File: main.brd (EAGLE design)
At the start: 53.3 x 68.6 mm, 36 parts, among them IC1 4050D, U1 MCP2551, U2 STN1100

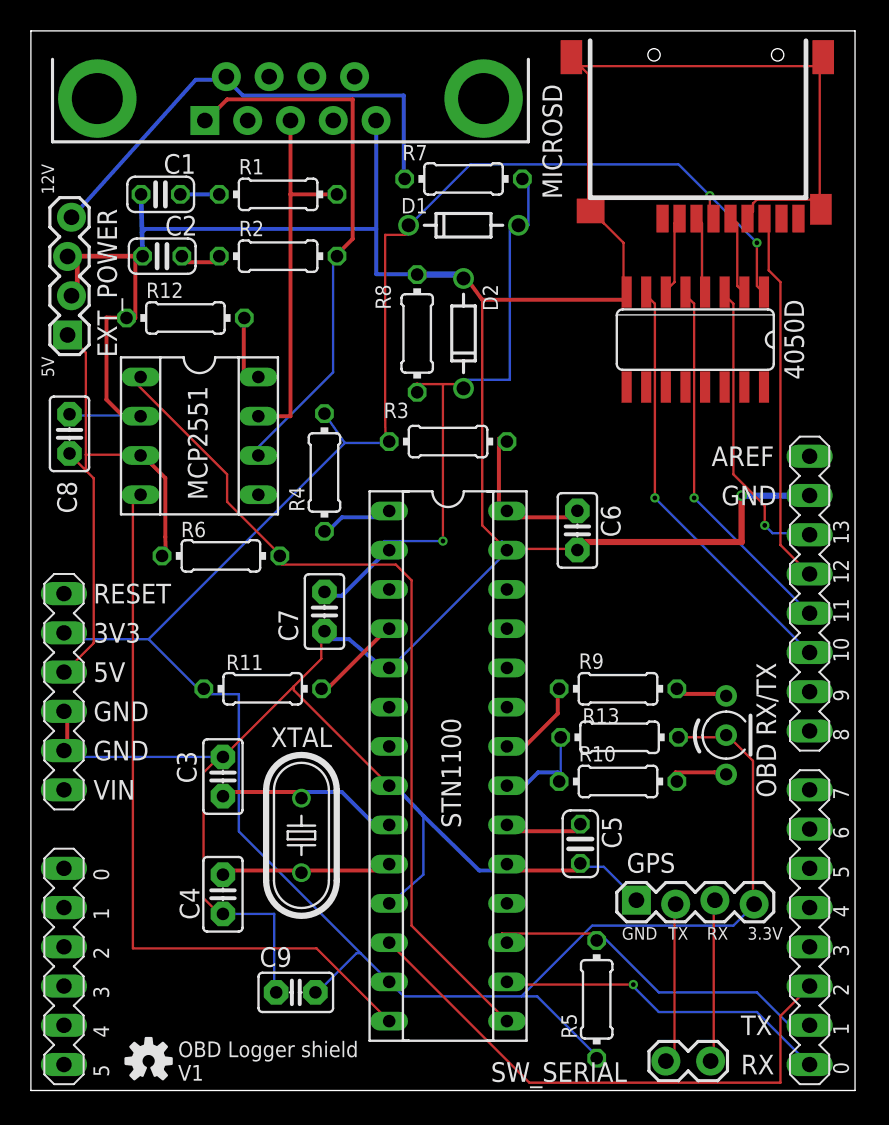
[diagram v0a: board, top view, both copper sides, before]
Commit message: Fixed errors on UART tx/rx
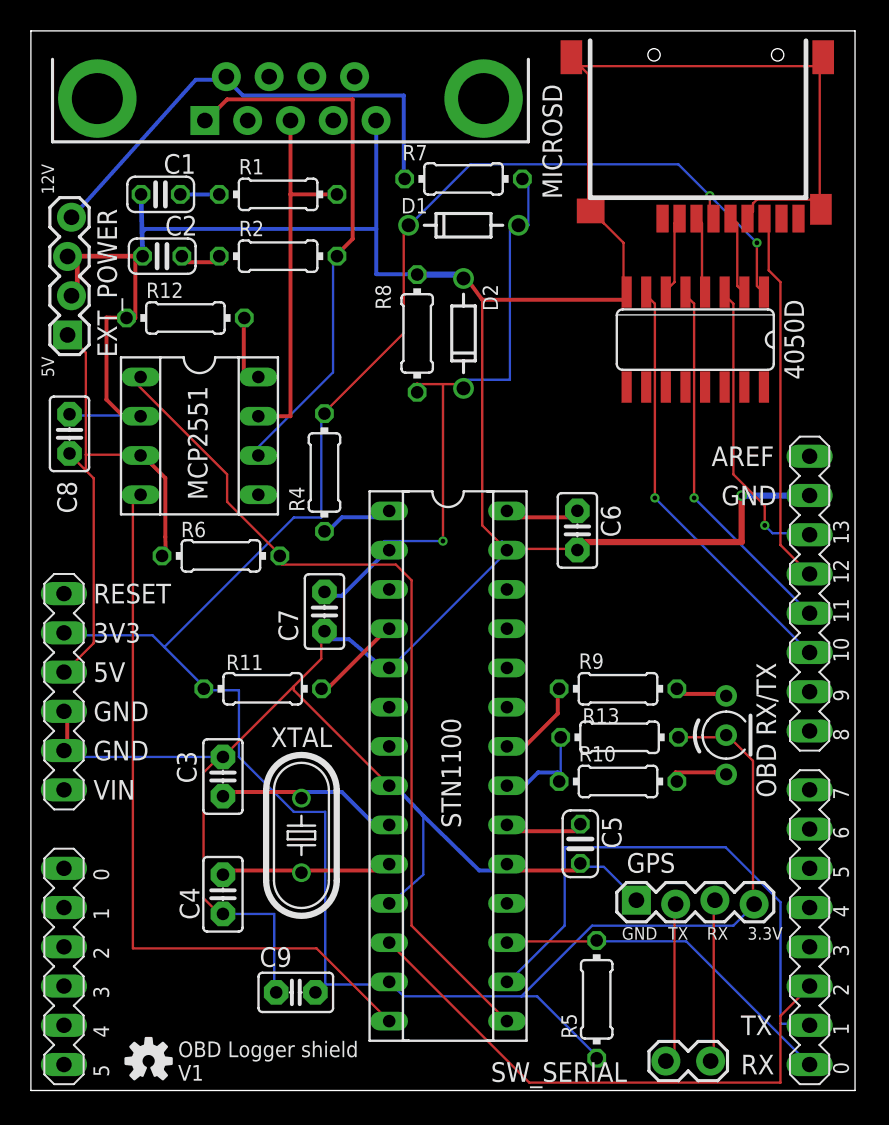
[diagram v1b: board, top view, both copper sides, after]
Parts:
- removed R3: 10, resistor:0204/7
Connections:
- net 3.3V: no longer R3.2
- net N$9: no longer R3.1
- net UART_RX: now also ARDUINO1.01; no longer ARDUINO1.00
- net UART_TX: now also ARDUINO1.00; no longer ARDUINO1.01
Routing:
- net UART_RX: track 21.9 -> 35.5 mm, vias 1 -> 0
- net N$9: track 11.4 -> 5.08 mm
- net 3.3V: track 158.6 -> 154.7 mm
- net UART_TX: track 24.3 -> 22.9 mm
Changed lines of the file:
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@@
 <element name="C5" library="rcl" package="C025-024X044" value="10uF" x="35.56" y="15.97" rot="R270"/>
 <element name="C6" library="capacitor-wima" package="C2.5-2" value="1uF" x="35.37" y="36.25" rot="R270"/>
-<element name="R3" library="resistor" package="0204/7" value="10" x="27" y="42" smashed="yes" rot="R180">
-<attribute name="NAME" x="24.46" y="44.5146" size="0.9906" layer="25" ratio="10" rot="R180"/>
-<attribute name="VALUE" x="28.6256" y="42.4826" size="0.9906" layer="27" ratio="10" rot="R180"/>
-</element>
 <element name="R4" library="resistor" package="0204/7" value="10k" x="19" y="40" rot="R90"/>
 <element name="R5" library="resistor" package="0204/7" value="1k" x="36.62" y="5.9" rot="R90"/>
@@
 <contactref element="ARDUINO1" pad="3V3"/>
 <contactref element="U2" pad="13"/>
-<contactref element="R3" pad="2"/>
 <contactref element="R4" pad="2"/>
 <contactref element="R5" pad="1"/>
@@
 <contactref element="IC1" pad="1"/>
 <contactref element="U$1" pad="4"/>
-<wire x1="7.62" y1="29.21" x2="11.176" y2="25.654" width="0.1524" layer="16"/>
-<wire x1="11.176" y1="25.654" x2="11.23" y2="25.6" width="0.1524" layer="16"/>
-<wire x1="2.54" y1="29.21" x2="7.62" y2="29.21" width="0.1524" layer="16"/>
-<wire x1="11.23" y1="25.6" x2="11.19" y2="26" width="0.1524" layer="16"/>
-<wire x1="2.54" y1="29.21" x2="2.14" y2="29.62" width="0.1524" layer="16"/>
-<wire x1="22.93" y1="43.48" x2="22.96" y2="41.91" width="0.1524" layer="1"/>
-<wire x1="22.93" y1="55.38" x2="22.93" y2="43.48" width="0.1524" layer="1"/>
-<wire x1="22.96" y1="41.91" x2="23.19" y2="42" width="0.1524" layer="1"/>
-<wire x1="22.93" y1="55.38" x2="24.4" y2="55.38" width="0.1524" layer="1"/>
-<wire x1="24.4" y1="55.38" x2="24.4" y2="55.8" width="0.1524" layer="1"/>
-<wire x1="24.4" y1="55.8" x2="24.444" y2="56" width="0.1524" layer="1"/>
-<wire x1="20.32" y1="41.91" x2="7.62" y2="29.21" width="0.1524" layer="16"/>
-<wire x1="22.86" y1="41.91" x2="20.32" y2="41.91" width="0.1524" layer="16"/>
-<wire x1="22.86" y1="41.91" x2="23.19" y2="42" width="0.1524" layer="16"/>
-<wire x1="20.32" y1="41.91" x2="19" y2="43.81" width="0.1524" layer="16"/>
-<wire x1="13.462" y1="16.764" x2="21.336" y2="8.89" width="0.1524" layer="16"/>
-<wire x1="21.336" y1="8.89" x2="23.114" y2="7.112" width="0.1524" layer="16"/>
-<wire x1="13.462" y1="25.654" x2="13.462" y2="16.764" width="0.1524" layer="16"/>
-<wire x1="11.176" y1="25.654" x2="13.462" y2="25.654" width="0.1524" layer="16"/>
-<wire x1="23.114" y1="7.112" x2="23.19" y2="7.03" width="0.1524" layer="16"/>
-<wire x1="11.176" y1="25.654" x2="11.19" y2="26" width="0.1524" layer="16"/>
 <wire x1="43.942" y1="57.912" x2="43.942" y2="56.642" width="0.1524" layer="1"/>
 <wire x1="41.91" y1="59.944" x2="43.942" y2="57.912" width="0.1524" layer="16"/>
@@
 <wire x1="46.736" y1="11.938" x2="46.81" y2="12.063" width="0.1524" layer="16"/>
 <contactref element="C9" pad="1"/>
-<wire x1="21.082" y1="8.89" x2="18.542" y2="6.35" width="0.1524" layer="16"/>
-<wire x1="21.336" y1="8.89" x2="21.082" y2="8.89" width="0.1524" layer="16"/>
+<wire x1="24.13" y1="49.022" x2="19.05" y2="43.942" width="0.1524" layer="1"/>
+<wire x1="24.13" y1="55.626" x2="24.13" y2="49.022" width="0.1524" layer="1"/>
+<wire x1="24.384" y1="55.88" x2="24.13" y2="55.626" width="0.1524" layer="1"/>
+<wire x1="19.05" y1="43.942" x2="19" y2="43.81" width="0.1524" layer="1"/>
+<wire x1="24.384" y1="55.88" x2="24.444" y2="56" width="0.1524" layer="1"/>
+<wire x1="19.05" y1="6.858" x2="18.542" y2="6.35" width="0.1524" layer="16"/>
+<wire x1="23.114" y1="6.858" x2="19.05" y2="6.858" width="0.1524" layer="16"/>
 <wire x1="18.542" y1="6.35" x2="18.415" y2="6.35" width="0.1524" layer="16"/>
+<wire x1="23.114" y1="6.858" x2="23.19" y2="7.03" width="0.1524" layer="16"/>
+<wire x1="7.874" y1="29.464" x2="8.636" y2="28.702" width="0.1524" layer="16"/>
+<wire x1="8.636" y1="28.702" x2="11.176" y2="26.162" width="0.1524" layer="16"/>
+<wire x1="2.286" y1="29.464" x2="7.874" y2="29.464" width="0.1524" layer="16"/>
+<wire x1="11.176" y1="26.162" x2="11.19" y2="26" width="0.1524" layer="16"/>
+<wire x1="2.286" y1="29.464" x2="2.14" y2="29.62" width="0.1524" layer="16"/>
+<wire x1="19.05" y1="18.034" x2="19.05" y2="6.858" width="0.1524" layer="16"/>
+<wire x1="17.018" y1="18.034" x2="19.05" y2="18.034" width="0.1524" layer="16"/>
+<wire x1="13.462" y1="21.59" x2="17.018" y2="18.034" width="0.1524" layer="16"/>
+<wire x1="13.462" y1="25.908" x2="13.462" y2="21.59" width="0.1524" layer="16"/>
+<wire x1="11.43" y1="25.908" x2="13.462" y2="25.908" width="0.1524" layer="16"/>
+<wire x1="11.43" y1="25.908" x2="11.19" y2="26" width="0.1524" layer="16"/>
+<wire x1="18.796" y1="37.084" x2="18.796" y2="43.688" width="0.1524" layer="16"/>
+<wire x1="17.018" y1="37.084" x2="18.796" y2="37.084" width="0.1524" layer="16"/>
+<wire x1="8.636" y1="28.702" x2="17.018" y2="37.084" width="0.1524" layer="16"/>
+<wire x1="18.796" y1="43.688" x2="19" y2="43.81" width="0.1524" layer="16"/>
 </signal>
 <signal name="CAN_TX">
@@
 <contactref element="C6" pad="1"/>
 <contactref element="U2" pad="28"/>
-<contactref element="R3" pad="1"/>
 <wire x1="35.37" y1="37.1" x2="31.56" y2="37.1" width="0.254" layer="1"/>
 <wire x1="31.56" y1="37.1" x2="30.81" y2="37.51" width="0.254" layer="1"/>
 <wire x1="35.37" y1="37.1" x2="35.37" y2="37.52" width="0.254" layer="1"/>
-<wire x1="30.29" y1="37.1" x2="30.29" y2="42.18" width="0.254" layer="1"/>
-<wire x1="30.29" y1="42.18" x2="30.81" y2="42" width="0.254" layer="1"/>
-<wire x1="30.29" y1="37.1" x2="30.81" y2="37.51" width="0.254" layer="1"/>
 </signal>
 <signal name="N$8">
@@
 <contactref element="U2" pad="17"/>
 <contactref element="R5" pad="2"/>
-<contactref element="ARDUINO1" pad="01"/>
-<wire x1="36.83" y1="10.16" x2="30.48" y2="10.16" width="0.1524" layer="1"/>
-<wire x1="30.48" y1="10.16" x2="30.81" y2="9.57" width="0.1524" layer="1"/>
-<wire x1="36.83" y1="10.16" x2="36.62" y2="9.71" width="0.1524" layer="1"/>
-<wire x1="46.99" y1="6.35" x2="49.53" y2="3.81" width="0.1524" layer="16"/>
-<wire x1="40.64" y1="6.35" x2="46.99" y2="6.35" width="0.1524" layer="16"/>
-<wire x1="36.83" y1="10.16" x2="40.64" y2="6.35" width="0.1524" layer="16"/>
-<wire x1="49.53" y1="3.81" x2="50.4" y2="4.22" width="0.1524" layer="16"/>
-<wire x1="36.83" y1="10.16" x2="36.62" y2="9.71" width="0.1524" layer="16"/>
+<contactref element="ARDUINO1" pad="00"/>
+<wire x1="36.576" y1="9.652" x2="30.988" y2="9.652" width="0.1524" layer="1"/>
+<wire x1="30.988" y1="9.652" x2="30.81" y2="9.57" width="0.1524" layer="1"/>
+<wire x1="36.576" y1="9.652" x2="36.62" y2="9.71" width="0.1524" layer="1"/>
+<wire x1="42.418" y1="9.652" x2="50.292" y2="1.778" width="0.1524" layer="16"/>
+<wire x1="36.83" y1="9.652" x2="42.418" y2="9.652" width="0.1524" layer="16"/>
+<wire x1="50.292" y1="1.778" x2="50.4" y2="1.68" width="0.1524" layer="16"/>
+<wire x1="36.83" y1="9.652" x2="36.62" y2="9.71" width="0.1524" layer="16"/>
 </signal>
 <signal name="UART_RX">
 <contactref element="U2" pad="16"/>
-<contactref element="ARDUINO1" pad="00"/>
-<wire x1="38.989" y1="6.858" x2="30.988" y2="6.858" width="0.1524" layer="1"/>
-<wire x1="30.988" y1="6.858" x2="30.81" y2="7.03" width="0.1524" layer="1"/>
-<via x="38.989" y="6.858" extent="1-16" drill="0.3048"/>
-<wire x1="38.989" y1="6.858" x2="38.989" y2="6.731" width="0.1524" layer="16"/>
-<wire x1="38.989" y1="6.731" x2="40.64" y2="5.08" width="0.1524" layer="16"/>
-<wire x1="40.64" y1="5.08" x2="46.99" y2="5.08" width="0.1524" layer="16"/>
-<wire x1="46.99" y1="5.08" x2="50.292" y2="1.778" width="0.1524" layer="16"/>
-<wire x1="50.292" y1="1.778" x2="50.4" y2="1.68" width="0.1524" layer="16"/>
+<contactref element="ARDUINO1" pad="01"/>
+<wire x1="34.544" y1="10.668" x2="30.988" y2="7.112" width="0.1524" layer="16"/>
+<wire x1="34.544" y1="15.748" x2="34.544" y2="10.668" width="0.1524" layer="16"/>
+<wire x1="44.958" y1="15.748" x2="34.544" y2="15.748" width="0.1524" layer="16"/>
+<wire x1="48.514" y1="12.192" x2="44.958" y2="15.748" width="0.1524" layer="16"/>
+<wire x1="48.514" y1="4.318" x2="48.514" y2="12.192" width="0.1524" layer="16"/>
+<wire x1="50.292" y1="4.318" x2="48.514" y2="4.318" width="0.1524" layer="16"/>
+<wire x1="30.988" y1="7.112" x2="30.81" y2="7.03" width="0.1524" layer="16"/>
+<wire x1="50.292" y1="4.318" x2="50.4" y2="4.22" width="0.1524" layer="16"/>
 </signal>
 <signal name="ANALOG_IN">
